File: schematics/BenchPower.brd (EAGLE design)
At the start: 80 x 67 mm, 31 parts, among them U1 V_REG_317SINK, X2 9090-4R

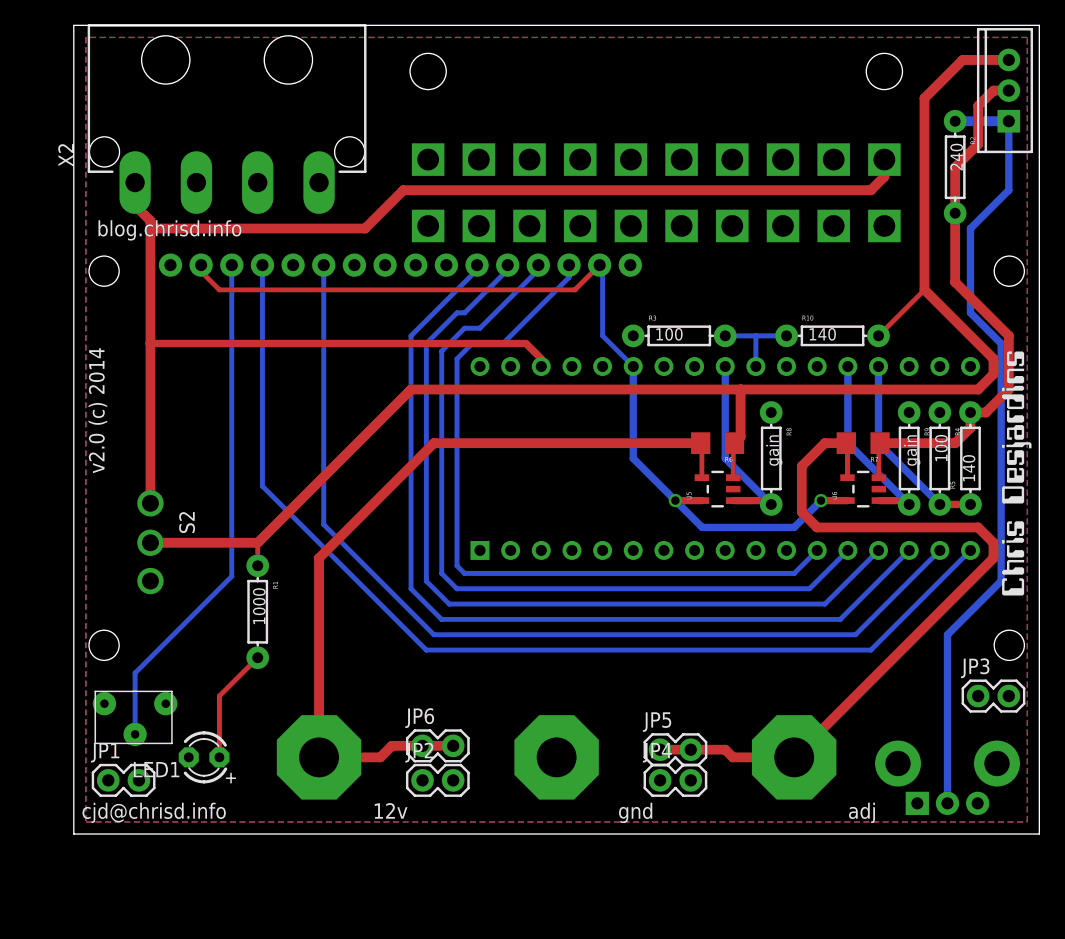
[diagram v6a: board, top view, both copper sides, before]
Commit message: Move pot off board, and other updates for v2.0
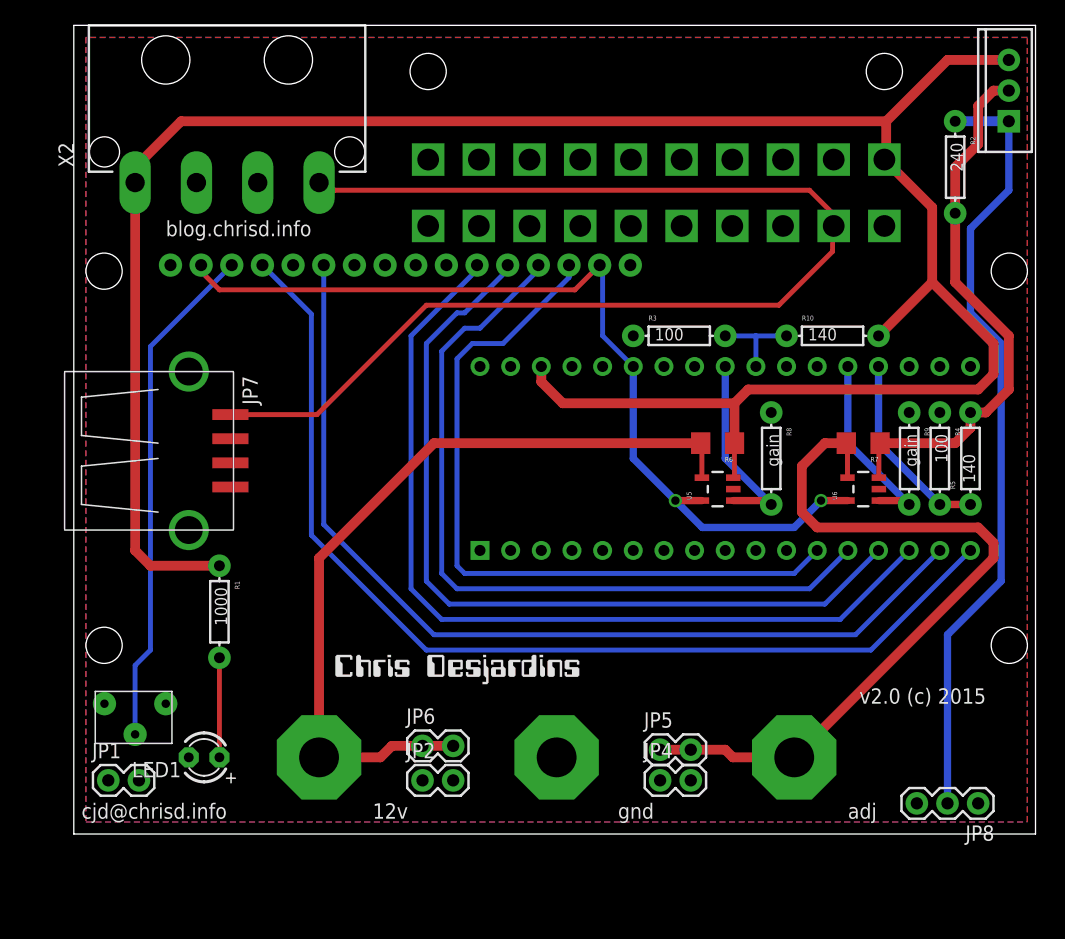
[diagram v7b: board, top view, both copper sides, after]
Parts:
- removed JP3: M02PTH, SparkFun-Connectors:1X02
- removed RV3: (no value), desjardins:POTRK09K111
- removed S2: EG1213, desjardins:EG1213
- added JP7: USB-A-S, SparkFun-Connectors:USB-A-S
- added JP8: (no value), SparkFun-Connectors:1X03
- moved U$3 57.5 mm to (21.6, 13.0), turned to 0 degrees
- moved R1 3.18 mm to (12.1, 18.4)
- renumbered U$1 to ATXCONN, U$2 to ARDUINOMICRO, U$4 to LCD
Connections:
- removed net 12VHDRSW: R1.P$1, R10.P$2, R6.1, S2.2, U1.IN, U5.3
- removed net 5V$3: ATXCONN.P$19
- new net 5VATX: ATXCONN.P$19, JP7.VBUS, X2.4
- net 12VHDR: now also R1.P$1, R10.P$2, R6.1, U1.IN, U5.3; no longer S2.1
- net ADJREG1: now also JP8.2; no longer RV3.P$2
- net GND: now also JP7.GND, JP8.1; no longer JP3.1, JP3.2, RV3.P$3
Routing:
- net 12VHDRSW: track 124.0 -> 0.00 mm
- net 5VATX: track 0.00 -> 102.3 mm
- net 12VHDR: track 124.7 -> 193.1 mm
- net N$1: track 9.57 -> 8.26 mm
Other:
- board size 80 x 67 mm -> 79.7 x 67 mm
- board text added: "v2.0 (c) 2015"
- board text removed: "v2.0 (c) 2014"

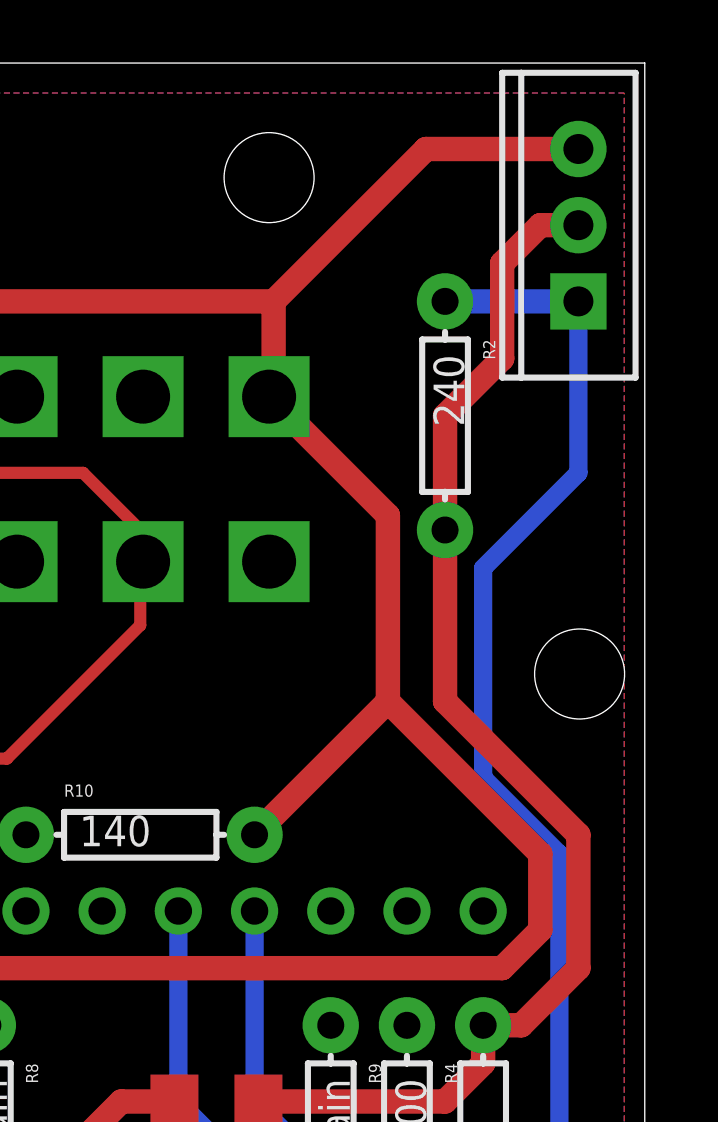
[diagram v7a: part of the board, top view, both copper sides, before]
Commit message: Flip the lm317 for heat sinking to the supply case
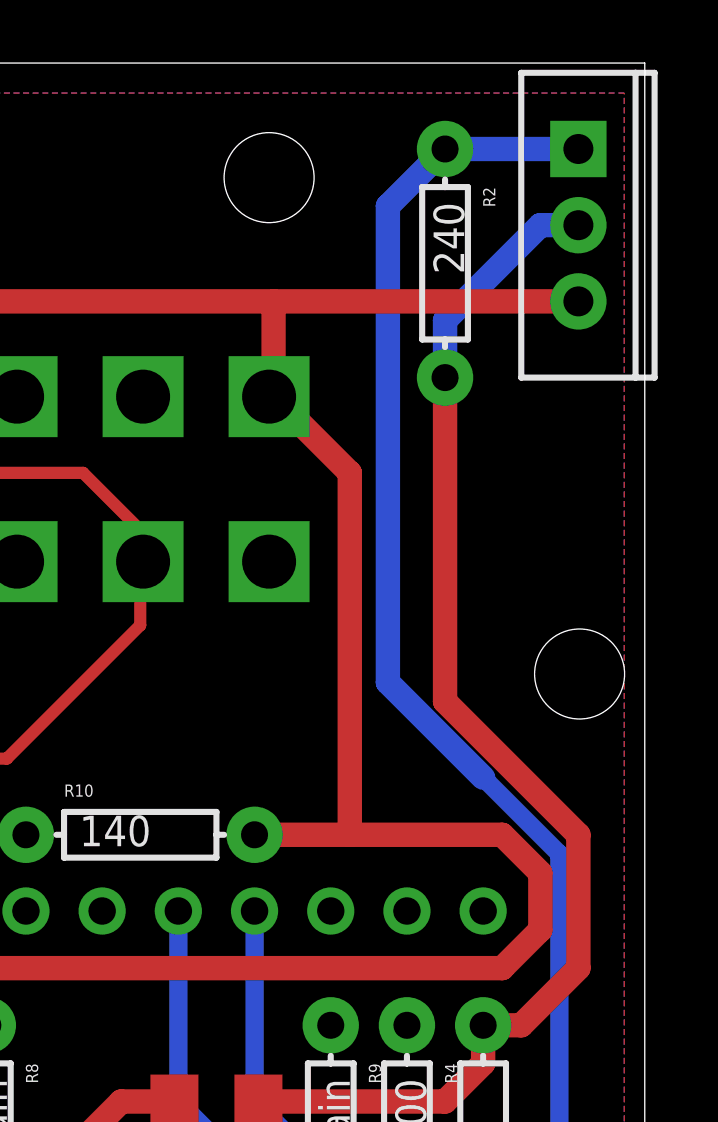
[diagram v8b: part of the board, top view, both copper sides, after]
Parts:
- moved R2 5.08 mm to (73.0, 60.3)
- turned U1 to 270 degrees
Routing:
- net ADJREG1: track 65.2 -> 71.0 mm
- net 12VHDR: track 193.1 -> 190.9 mm
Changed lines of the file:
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@@
 <element name="ATXCONN" library="desjardins" package="ATXPOWER" value="ATXPOWER" x="48.26" y="55.88" rot="R270"/>
 <element name="ARDUINOMICRO" library="ChrisD" package="ARDUINO_PRO_MICRO" value="ARDUINO_PRO_MICRO" x="78.105" y="22.225" rot="R90"/>
-<element name="U1" library="SparkFun-PowerIC" package="TO220-ADJ" value="V_REG_317SINK" x="77.47" y="61.595" rot="R90"/>
+<element name="U1" library="SparkFun-PowerIC" package="TO220-ADJ" value="V_REG_317SINK" x="77.47" y="61.595" rot="R270"/>
 <element name="R1" library="SparkFun-Passives" package="AXIAL-0.3" value="1000" x="12.065" y="18.415" rot="R270"/>
-<element name="R2" library="SparkFun-Passives" package="AXIAL-0.3" value="240" x="73.025" y="55.245" rot="R270"/>
+<element name="R2" library="SparkFun-Passives" package="AXIAL-0.3" value="240" x="73.025" y="60.325" rot="R270"/>
 <element name="U$3" library="desjardins" package="LOGO" value="" x="21.59" y="13.0175"/>
 <element name="LCD" library="desjardins" package="DT162C" value="16X2LCDDT162C" x="40.01" y="31.135"/>
@@
 <wire x1="54.74" y1="32.385" x2="54.74" y2="35.69" width="0.8128" layer="1"/>
 <wire x1="54.74" y1="35.69" x2="55.88" y2="36.83" width="0.8128" layer="1"/>
-<wire x1="77.47" y1="64.135" x2="72.39" y2="64.135" width="0.8128" layer="1"/>
-<wire x1="71.12" y1="45.72" x2="71.12" y2="51.92" width="0.8128" layer="1"/>
-<wire x1="71.12" y1="45.72" x2="76.2" y2="40.64" width="0.8128" layer="1"/>
-<wire x1="76.2" y1="40.64" x2="76.2" y2="38.1" width="0.8128" layer="1"/>
 <wire x1="76.2" y1="38.1" x2="74.93" y2="36.83" width="0.8128" layer="1"/>
 <wire x1="74.93" y1="36.83" x2="55.88" y2="36.83" width="0.8128" layer="1"/>
-<wire x1="66.675" y1="41.275" x2="71.12" y2="45.72" width="0.8128" layer="1"/>
 <wire x1="54.74" y1="35.69" x2="40.51" y2="35.69" width="0.8128" layer="1"/>
 <wire x1="40.51" y1="35.69" x2="38.735" y2="37.465" width="0.8128" layer="1"/>
@@
 <wire x1="8.89" y1="59.055" x2="5.08" y2="55.245" width="0.8128" layer="1"/>
 <wire x1="5.08" y1="55.245" x2="5.08" y2="53.975" width="0.8128" layer="1"/>
-<wire x1="71.12" y1="51.92" x2="67.16" y2="55.88" width="0.8128" layer="1"/>
-<wire x1="72.39" y1="64.135" x2="67.31" y2="59.055" width="0.8128" layer="1"/>
 <wire x1="67.31" y1="59.055" x2="67.31" y2="56.03" width="0.8128" layer="1"/>
 <wire x1="67.31" y1="56.03" x2="67.16" y2="55.88" width="0.8128" layer="1"/>
+<wire x1="67.16" y1="55.88" x2="67.31" y2="55.88" width="0.8128" layer="1"/>
+<wire x1="67.31" y1="55.88" x2="69.85" y2="53.34" width="0.8128" layer="1"/>
+<wire x1="69.85" y1="53.34" x2="69.85" y2="41.275" width="0.8128" layer="1"/>
+<wire x1="66.675" y1="41.275" x2="69.85" y2="41.275" width="0.8128" layer="1"/>
+<wire x1="69.85" y1="41.275" x2="74.93" y2="41.275" width="0.8128" layer="1"/>
+<wire x1="74.93" y1="41.275" x2="76.2" y2="40.005" width="0.8128" layer="1"/>
+<wire x1="76.2" y1="40.005" x2="76.2" y2="38.1" width="0.8128" layer="1"/>
+<wire x1="77.47" y1="59.055" x2="67.31" y2="59.055" width="0.8128" layer="1"/>
 </signal>
 <signal name="N$1">
@@
 <wire x1="73.025" y1="32.385" x2="74.295" y2="33.655" width="0.8128" layer="1"/>
 <wire x1="74.295" y1="33.655" x2="74.295" y2="34.925" width="0.8128" layer="1"/>
-<wire x1="73.025" y1="51.435" x2="73.025" y2="55.245" width="0.8128" layer="1"/>
-<wire x1="73.025" y1="55.245" x2="74.93" y2="57.15" width="0.8128" layer="1"/>
-<wire x1="74.93" y1="57.15" x2="74.93" y2="60.325" width="0.8128" layer="1"/>
-<wire x1="74.93" y1="60.325" x2="76.2" y2="61.595" width="0.8128" layer="1"/>
-<wire x1="76.2" y1="61.595" x2="77.47" y2="61.595" width="0.8128" layer="1"/>
 <wire x1="74.295" y1="34.925" x2="75.565" y2="34.925" width="0.8128" layer="1"/>
 <wire x1="75.565" y1="34.925" x2="77.47" y2="36.83" width="0.8128" layer="1"/>
 <wire x1="77.47" y1="36.83" x2="77.47" y2="41.275" width="0.8128" layer="1"/>
 <wire x1="77.47" y1="41.275" x2="73.025" y2="45.72" width="0.8128" layer="1"/>
-<wire x1="73.025" y1="45.72" x2="73.025" y2="51.435" width="0.8128" layer="1"/>
+<wire x1="73.025" y1="45.72" x2="73.025" y2="56.515" width="0.8128" layer="1"/>
+<wire x1="73.025" y1="56.515" x2="73.025" y2="58.42" width="0.8128" layer="16"/>
+<wire x1="73.025" y1="58.42" x2="76.2" y2="61.595" width="0.8128" layer="16"/>
+<wire x1="76.2" y1="61.595" x2="77.47" y2="61.595" width="0.8128" layer="16"/>
 </signal>
 <signal name="ADJREG1">
 <contactref element="U1" pad="ADJ"/>
 <contactref element="R2" pad="P$1"/>
-<wire x1="73.025" y1="59.055" x2="77.47" y2="59.055" width="0.8128" layer="16"/>
-<wire x1="74.295" y1="50.165" x2="77.47" y2="53.34" width="0.6096" layer="16"/>
-<wire x1="77.47" y1="53.34" x2="77.47" y2="59.055" width="0.6096" layer="16"/>
-<wire x1="74.295" y1="50.165" x2="74.295" y2="43.18" width="0.6096" layer="16"/>
 <wire x1="74.295" y1="43.18" x2="76.835" y2="40.64" width="0.6096" layer="16"/>
 <wire x1="76.835" y1="40.64" x2="76.835" y2="20.955" width="0.6096" layer="16"/>
@@
 <wire x1="76.835" y1="20.955" x2="72.39" y2="16.51" width="0.6096" layer="16"/>
 <wire x1="72.39" y1="16.51" x2="72.39" y2="2.54" width="0.6096" layer="16"/>
+<wire x1="73.025" y1="64.135" x2="77.47" y2="64.135" width="0.8128" layer="16"/>
+<wire x1="74.295" y1="43.18" x2="71.12" y2="46.355" width="0.8128" layer="16"/>
+<wire x1="71.12" y1="46.355" x2="71.12" y2="62.23" width="0.8128" layer="16"/>
+<wire x1="71.12" y1="62.23" x2="73.025" y2="64.135" width="0.8128" layer="16"/>
 </signal>
 <signal name="5VARDU">
